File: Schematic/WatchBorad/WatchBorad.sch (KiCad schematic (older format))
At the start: 42 parts, among them IC1 TXS0108E, J1 Conn_01x06_Male, J2 Conn_01x09_Female, J3 USB_B_Mini, J4 Conn_01x10_Female, J5 Conn_01x06_Female, J6 Conn_01x04_Male, SW1 SW_Push, SW2 SW_Push, U1 E73-2G4M04S-52832, U2 FH26-13S-0.3SHW(05), U3 W25Q16BVSSIG, U5 MCP1700-3302E_SOT23, U6 MCP1700-1802E_SOT23, U7 LP2985-2.8, U8 MPU-9250

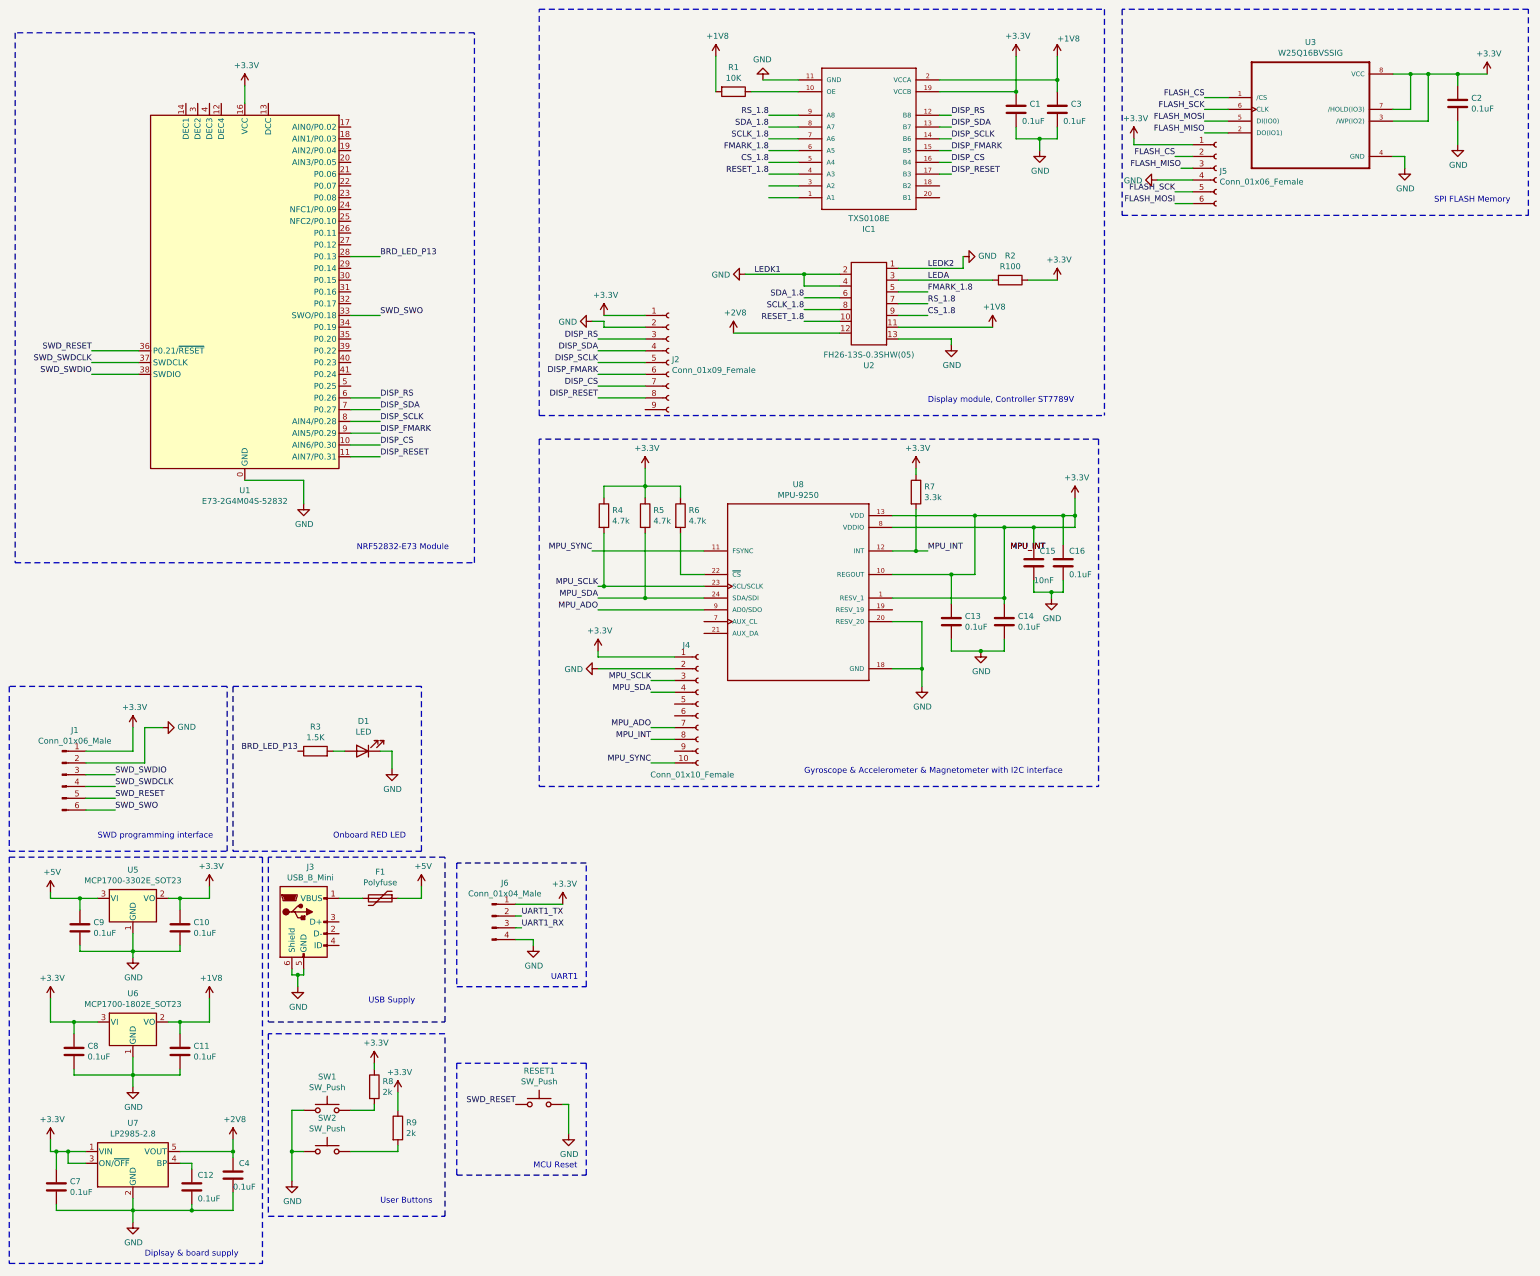
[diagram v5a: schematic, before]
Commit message: Added connectors for top-board
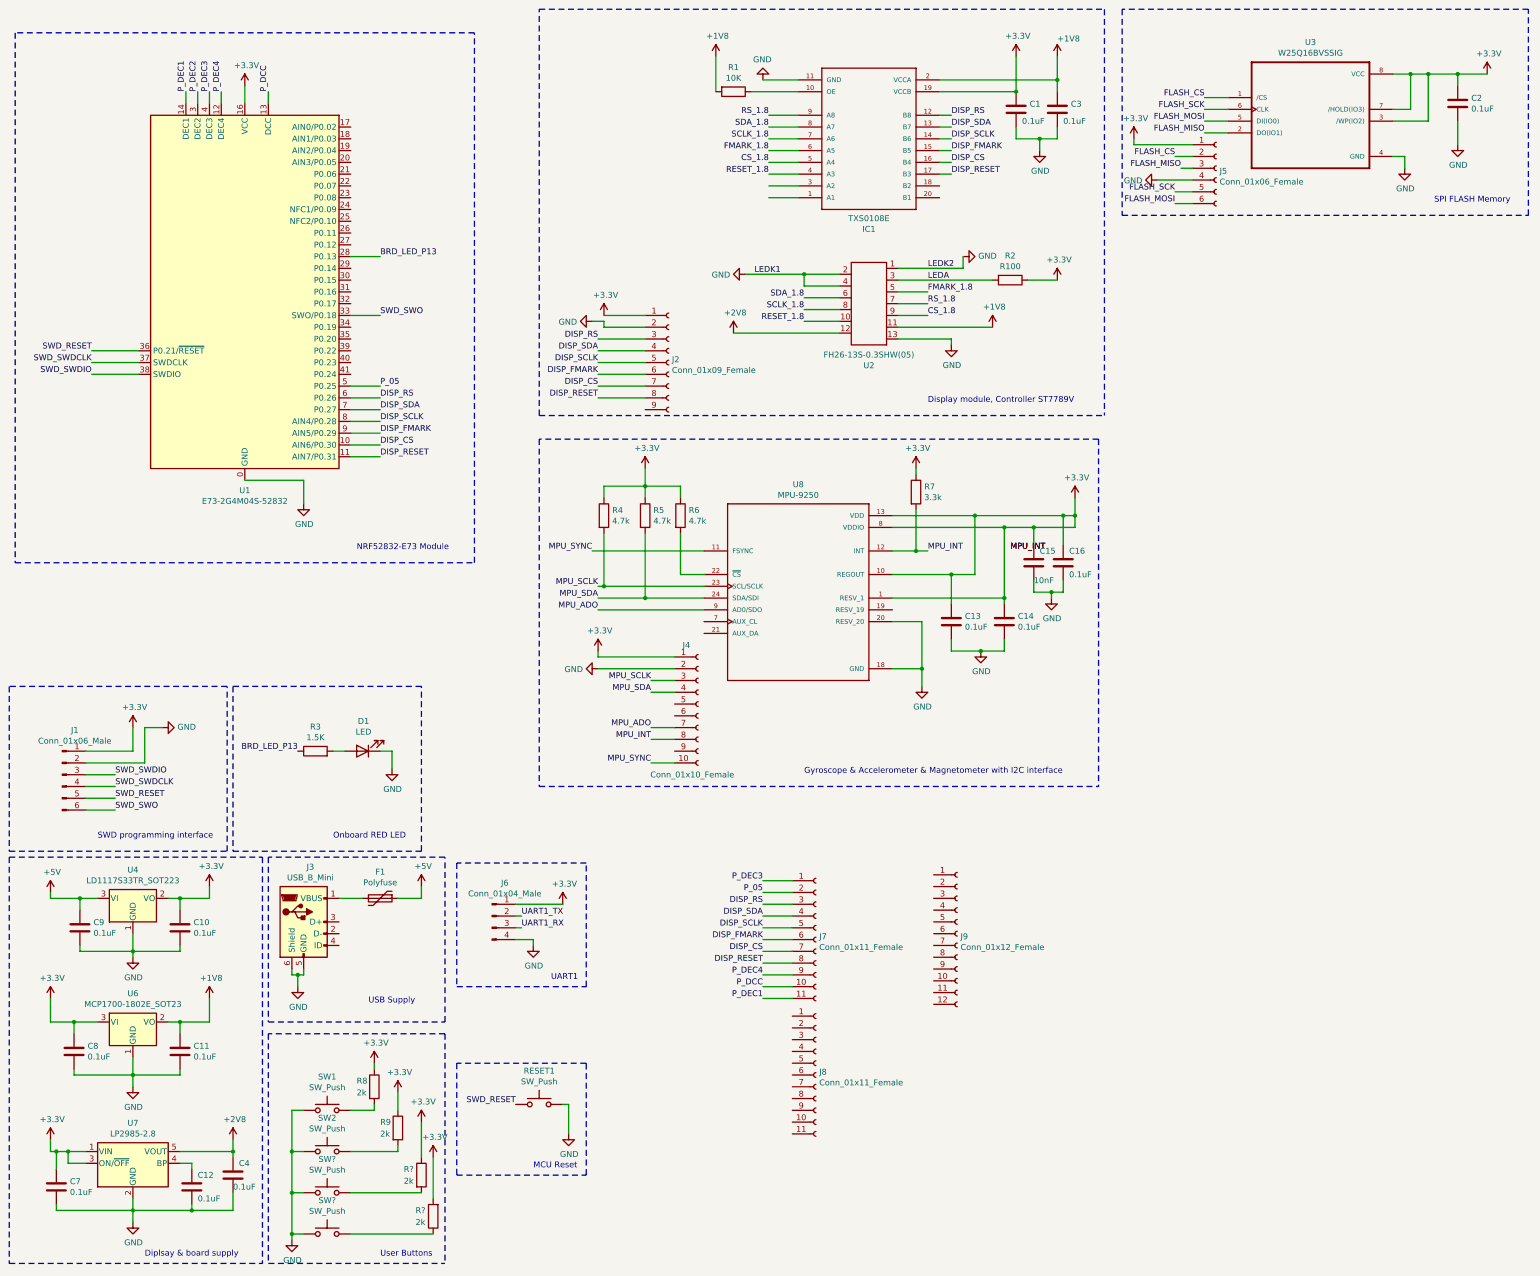
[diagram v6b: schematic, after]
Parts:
- removed U5: MCP1700-3302E_SOT23, Package_TO_SOT_SMD:SOT-23, symbol Regulator_Linear:MCP1700-3302E_SOT23
- added J7, J8: Conn_01x11_Female, Connector_PinSocket_2.54mm:PinSocket_1x11_P2.54mm_Vertical, symbol Connector:Conn_01x11_Female
- added J9: Conn_01x12_Female, Connector_PinSocket_2.54mm:PinSocket_1x12_P2.54mm_Vertical, symbol Connector:Conn_01x12_Female
- added R? (x2): 2k, Resistor_SMD:R_0805_2012Metric_Pad1.15x1.40mm_HandSolder, symbol Device:R
- added SW? (x2): SW_Push, Button_Switch_SMD:SW_SPST_SKQG_WithStem, symbol Switch:SW_Push
- added U4: LD1117S33TR_SOT223, Package_TO_SOT_SMD:SOT-223-3_TabPin2, symbol Regulator_Linear:LD1117S33TR_SOT223
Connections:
- net +3V3: now also R?.1, R?.2, U4.2 (VO)
- net +5V: now also U4.3 (VI)
- net DISP_CS: now also J7.7 (Pin_7)
- net DISP_FMARK: now also J7.6 (Pin_6)
- net DISP_RESET: now also J7.8 (Pin_8)
- net DISP_RS: now also J7.3 (Pin_3)
- net DISP_SCLK: now also J7.5 (Pin_5)
- net DISP_SDA: now also J7.4 (Pin_4)
- net GND: now also SW?.1, SW?.1, U4.1 (GND)
- net P_DEC4: now reaches U1.12 (DEC4)
- net P_DEC4: now also J7.9 (Pin_9)
- net P_DCC: now reaches U1.13 (DCC)
- net P_DCC: now also J7.10 (Pin_10)
- net P_DEC1: now reaches U1.14 (DEC1)
- net P_DEC1: now also J7.11 (Pin_11)
- net P_DEC2: now reaches U1.3 (DEC2)
- net P_DEC3: now reaches U1.4 (DEC3)
- net P_DEC3: now also J7.1 (Pin_1)
- net P_05: now reaches U1.5 (P0.25)
- net P_05: now also J7.2 (Pin_2)
- new net: R?.2, SW?.2
- new net: R?.1, SW?.2
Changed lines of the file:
@@
 EESchema Schematic File Version 4
+LIBS:WatchBorad-cache
 EELAYER 30 0
 EELAYER END
@@
 	1    0    0    -1
 $EndComp
-$Comp
-L Regulator_Linear:MCP1700-3302E_SOT23 U5
-U 1 1 5DBB69D4
-P 1650 8100
-F 0 "U5" H 1650 8342 50  0000 C CNN
-F 1 "MCP1700-3302E_SOT23" H 1650 8251 50  0000 C CNN
-F 2 "Package_TO_SOT_SMD:SOT-23" H 1650 8325 50  0001 C CNN
-F 3 "http://ww1.microchip.com/downloads/en/DeviceDoc/20001826C.pdf" H 1650 8100 50  0001 C CNN
-	1    1650 8100
-	1    0    0    -1
-$EndComp
 Wire Notes Line
 	4100 6300 2500 6300
@@
 U 1 1 5E659671
 P 3700 9700
-F 0 "R8" H 3770 9746 50  0000 L CNN
-F 1 "2k" H 3770 9655 50  0000 L CNN
+F 0 "R8" H 3550 9750 50  0000 L CNN
+F 1 "2k" H 3550 9650 50  0000 L CNN
 F 2 "Resistor_SMD:R_0805_2012Metric_Pad1.15x1.40mm_HandSolder" V 3630 9700 50  0001 C CNN
 F 3 "~" H 3700 9700 50  0001 C CNN
@@
 L power:GND #PWR0136
 U 1 1 5E67A207
-P 3000 10500
-F 0 "#PWR0136" H 3000 10250 50  0001 C CNN
-F 1 "GND" H 3005 10327 50  0000 C CNN
-F 2 "" H 3000 10500 50  0001 C CNN
-F 3 "" H 3000 10500 50  0001 C CNN
-	1    3000 10500
+P 3000 11000
+F 0 "#PWR0136" H 3000 10750 50  0001 C CNN
+F 1 "GND" H 3005 10827 50  0000 C CNN
+F 2 "" H 3000 11000 50  0001 C CNN
+F 3 "" H 3000 11000 50  0001 C CNN
+	1    3000 11000
 	1    0    0    -1
 $EndComp
@@
 U 1 1 5E6ACBD3
 P 3900 10050
-F 0 "R9" H 3970 10096 50  0000 L CNN
-F 1 "2k" H 3970 10005 50  0000 L CNN
+F 0 "R9" H 3750 10100 50  0000 L CNN
+F 1 "2k" H 3750 10000 50  0000 L CNN
 F 2 "Resistor_SMD:R_0805_2012Metric_Pad1.15x1.40mm_HandSolder" V 3830 10050 50  0001 C CNN
 F 3 "~" H 3900 10050 50  0001 C CNN
@@
 	3000 9900 3000 10250
 Connection ~ 3000 10250
-Wire Wire Line
-	3000 10250 3000 10500
 $Comp
 L power:GND #PWR0148
@@
 USB Supply
 Wire Notes Line
-	2800 9250 2800 10800
-Wire Notes Line
-	2800 10800 4300 10800
-Wire Notes Line
-	4300 10800 4300 9250
+	2800 11200 4300 11200
 Wire Notes Line
 	4300 9250 2800 9250
-Text Notes 3750 10700 0    50   ~ 0
+Text Notes 3750 11150 0    50   ~ 0
 User Buttons
 Wire Notes Line
@@
 Text Notes 3550 5150 0    50   ~ 0
 NRF52832-E73 Module
+$Comp
+L Regulator_Linear:LD1117S33TR_SOT223 U4
+U 1 1 5DB6B184
+P 1650 8100
+F 0 "U4" H 1650 8342 50  0000 C CNN
+F 1 "LD1117S33TR_SOT223" H 1650 8251 50  0000 C CNN
+F 2 "Package_TO_SOT_SMD:SOT-223-3_TabPin2" H 1650 8300 50  0001 C CNN
+F 3 "http://www.st.com/st-web-ui/static/active/en/resource/technical/document/datasheet/CD00000544.pdf" H 1750 7850 50  0001 C CNN
+	1    1650 8100
+	1    0    0    -1
+$EndComp
+$Comp
+L Connector:Conn_01x11_Female J7
+U 1 1 5DB988BA
+P 7450 8450
+F 0 "J7" H 7478 8476 50  0000 L CNN
+F 1 "Conn_01x11_Female" H 7478 8385 50  0000 L CNN
+F 2 "Connector_PinSocket_2.54mm:PinSocket_1x11_P2.54mm_Vertical" H 7450 8450 50  0001 C CNN
+F 3 "~" H 7450 8450 50  0001 C CNN
+	1    7450 8450
+	1    0    0    -1
+$EndComp
+$Comp
+L Connector:Conn_01x11_Female J8
+U 1 1 5DB9DBB8
+P 7450 9600
+F 0 "J8" H 7478 9626 50  0000 L CNN
+F 1 "Conn_01x11_Female" H 7478 9535 50  0000 L CNN
+F 2 "Connector_PinSocket_2.54mm:PinSocket_1x11_P2.54mm_Vertical" H 7450 9600 50  0001 C CNN
+F 3 "~" H 7450 9600 50  0001 C CNN
+	1    7450 9600
+	1    0    0    -1
+$EndComp
+$Comp
+L Connector:Conn_01x12_Female J9
+U 1 1 5DBA0F85
+P 8650 8400
+F 0 "J9" H 8678 8376 50  0000 L CNN
+F 1 "Conn_01x12_Female" H 8678 8285 50  0000 L CNN
+F 2 "Connector_PinSocket_2.54mm:PinSocket_1x12_P2.54mm_Vertical" H 8650 8400 50  0001 C CNN
+F 3 "~" H 8650 8400 50  0001 C CNN
+	1    8650 8400
+	1    0    0    -1
+$EndComp
+Text Label 2100 1250 1    50   ~ 0
+P_DEC1
+Wire Wire Line
+	2100 1250 2100 1350
+Text Label 2200 1250 1    50   ~ 0
+P_DEC2
+Text Label 2300 1250 1    50   ~ 0
+P_DEC3
+Text Label 2400 1250 1    50   ~ 0
+P_DEC4
+Wire Wire Line
+	2400 1250 2400 1350
+Wire Wire Line
+	2300 1250 2300 1350
+Wire Wire Line
+	2200 1350 2200 1250
+Text Label 7000 8950 2    50   ~ 0
+P_DEC1
+Wire Wire Line
+	7000 8950 7250 8950
+Text Label 2800 1250 1    50   ~ 0
+P_DCC
+Wire Wire Line
+	2800 1250 2800 1350
+Text Label 7000 8850 2    50   ~ 0
+P_DCC
+Wire Wire Line
+	7000 8850 7250 8850
+Text Label 7000 8750 2    50   ~ 0
+P_DEC4
+Wire Wire Line
+	7000 8750 7250 8750
+Text Label 7000 8650 2    50   ~ 0
+DISP_RESET
+Wire Wire Line
+	7000 8650 7250 8650
+Text Label 7000 8550 2    50   ~ 0
+DISP_CS
+Wire Wire Line
+	7000 8550 7250 8550
+Text Label 7000 8450 2    50   ~ 0
+DISP_FMARK
+Wire Wire Line
+	7000 8450 7250 8450
+Text Label 7000 8350 2    50   ~ 0
+DISP_SCLK
+Wire Wire Line
+	7000 8350 7250 8350
+Text Label 7000 8250 2    50   ~ 0
+DISP_SDA
+Wire Wire Line
+	7000 8250 7250 8250
+Text Label 7000 8150 2    50   ~ 0
+DISP_RS
+Wire Wire Line
+	7000 8150 7250 8150
+Text Label 3750 3750 0    50   ~ 0
+P_05
+Wire Wire Line
+	3500 3750 3750 3750
+Text Label 7000 8050 2    50   ~ 0
+P_05
+Wire Wire Line
+	7250 8050 7000 8050
+Text Label 7000 7950 2    50   ~ 0
+P_DEC3
+Wire Wire Line
+	7000 7950 7250 7950
+$Comp
+L Switch:SW_Push SW?
+U 1 1 5DD80B15
+P 3300 10600
+F 0 "SW?" H 3300 10885 50  0000 C CNN
+F 1 "SW_Push" H 3300 10794 50  0000 C CNN
+F 2 "Button_Switch_SMD:SW_SPST_SKQG_WithStem" H 3300 10800 50  0001 C CNN
+F 3 "~" H 3300 10800 50  0001 C CNN
+	1    3300 10600
+	1    0    0    -1
+$EndComp
+$Comp
+L Switch:SW_Push SW?
+U 1 1 5DD80B1B
+P 3300 10950
+F 0 "SW?" H 3300 11235 50  0000 C CNN
+F 1 "SW_Push" H 3300 11144 50  0000 C CNN
+F 2 "Button_Switch_SMD:SW_SPST_SKQG_WithStem" H 3300 11150 50  0001 C CNN
+F 3 "~" H 3300 11150 50  0001 C CNN
+	1    3300 10950
+	1    0    0    -1
+$EndComp
+Wire Wire Line
+	3000 10250 3000 10600
+Wire Notes Line
+	2800 9250 2800 11200
+Wire Notes Line
+	4300 9250 4300 11200
+$Comp
+L Device:R R?
+U 1 1 5DDFA376
+P 4100 10450
+F 0 "R?" H 3950 10500 50  0000 L CNN
+F 1 "2k" H 3950 10400 50  0000 L CNN
+F 2 "Resistor_SMD:R_0805_2012Metric_Pad1.15x1.40mm_HandSolder" V 4030 10450 50  0001 C CNN
+F 3 "~" H 4100 10450 50  0001 C CNN
+	1    4100 10450
+	1    0    0    -1
+$EndComp
+$Comp
+L Device:R R?
+U 1 1 5DDFB2BF
+P 4200 10800
+F 0 "R?" H 4350 10750 50  0000 R CNN
+F 1 "2k" H 4350 10850 50  0000 R CNN
+F 2 "Resistor_SMD:R_0805_2012Metric_Pad1.15x1.40mm_HandSolder" V 4130 10800 50  0001 C CNN
+F 3 "~" H 4200 10800 50  0001 C CNN
+	1    4200 10800
+	-1   0    0    1
+$EndComp
+Wire Wire Line
+	3500 10600 4100 10600
+Wire Wire Line
+	3500 10950 4200 10950
+Wire Wire Line
+	3100 10950 3000 10950
+Connection ~ 3000 10950
+Wire Wire Line
+	3000 10950 3000 11000
+Wire Wire Line
+	3100 10600 3000 10600
+Connection ~ 3000 10600
+Wire Wire Line
+	3000 10600 3000 10950
+$Comp
+L power:+3.3V #PWR?
+U 1 1 5DE52393
+P 4100 10000
+F 0 "#PWR?" H 4100 9850 50  0001 C CNN
+F 1 "+3.3V" H 4115 10173 50  0000 C CNN
+F 2 "" H 4100 10000 50  0001 C CNN
+F 3 "" H 4100 10000 50  0001 C CNN
+	1    4100 10000
+	1    0    0    -1
+$EndComp
+$Comp
+L power:+3.3V #PWR?
+U 1 1 5DE52E80
+P 4200 10300
+F 0 "#PWR?" H 4200 10150 50  0001 C CNN
+F 1 "+3.3V" H 4215 10473 50  0000 C CNN
+F 2 "" H 4200 10300 50  0001 C CNN
+F 3 "" H 4200 10300 50  0001 C CNN
+	1    4200 10300
+	1    0    0    -1
+$EndComp
+Wire Wire Line
+	4200 10300 4200 10650
+Wire Wire Line
+	4100 10300 4100 10000
 $EndSCHEMATC

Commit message: Added connectors for top-board-schematic
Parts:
- removed C1, C10, C11, C12, C13, C14, C16, C2, C3, C4, C7, C8, C9: 0.1uF, Capacitor_SMD:C_0805_2012Metric_Pad1.15x1.40mm_HandSolder, symbol Device:C
- removed C15: 10nF, Capacitor_SMD:C_0805_2012Metric_Pad1.15x1.40mm_HandSolder, symbol Device:C
- removed D1: LED, LED_SMD:LED_0805_2012Metric_Pad1.15x1.40mm_HandSolder, symbol Device:LED
- removed F1: Polyfuse, Fuse:Fuse_1206_3216Metric_Pad1.42x1.75mm_HandSolder, symbol Device:Polyfuse
- removed IC1: TXS0108E, TXS0108E:PW_R-PDSO-G20, symbol TXS0108E:TXS0108E
- removed J1: Conn_01x06_Male, Connector_PinHeader_2.54mm:PinHeader_1x06_P2.54mm_Vertical, symbol Connector:Conn_01x06_Male
- removed J2: Conn_01x09_Female, Connector_PinSocket_2.54mm:PinSocket_1x09_P2.54mm_Vertical, symbol Connector:Conn_01x09_Female
- removed J3: USB_B_Mini, Connector_USB:USB_Mini-B_Lumberg_2486_01_Horizontal, symbol Connector:USB_B_Mini
- removed J4: Conn_01x10_Female, Connector_PinSocket_2.54mm:PinSocket_1x10_P2.54mm_Vertical, symbol Connector:Conn_01x10_Female
- removed J5: Conn_01x06_Female, Connector_PinSocket_2.54mm:PinSocket_1x06_P2.54mm_Vertical, symbol Connector:Conn_01x06_Female
- removed J6: Conn_01x04_Male, Connector_PinHeader_2.54mm:PinHeader_1x04_P2.54mm_Vertical, symbol Connector:Conn_01x04_Male
- removed J7, J8: Conn_01x11_Female, Connector_PinSocket_2.54mm:PinSocket_1x11_P2.54mm_Vertical, symbol Connector:Conn_01x11_Female
- removed J9: Conn_01x12_Female, Connector_PinSocket_2.54mm:PinSocket_1x12_P2.54mm_Vertical, symbol Connector:Conn_01x12_Female
- removed R1: 10K, Resistor_SMD:R_0805_2012Metric_Pad1.15x1.40mm_HandSolder, symbol Device:R
- removed R2: R100, Resistor_SMD:R_0805_2012Metric_Pad1.15x1.40mm_HandSolder, symbol Device:R
- removed R3: 1.5K, Resistor_SMD:R_0805_2012Metric_Pad1.15x1.40mm_HandSolder, symbol Device:R
- removed R4, R5, R6: 4.7k, Resistor_SMD:R_0805_2012Metric_Pad1.15x1.40mm_HandSolder, symbol Device:R
- removed R7: 3.3k, Resistor_SMD:R_0805_2012Metric_Pad1.15x1.40mm_HandSolder, symbol Device:R
- removed R8, R9, R? (x2): 2k, Resistor_SMD:R_0805_2012Metric_Pad1.15x1.40mm_HandSolder, symbol Device:R
- removed RESET1, SW1, SW2, SW? (x2): SW_Push, Button_Switch_SMD:SW_SPST_SKQG_WithStem, symbol Switch:SW_Push
- removed U1: E73-2G4M04S-52832, RF_Module:E73-2G4M04S, symbol RF_Module:E73-2G4M04S-52832
- removed U2: FH26-13S-0.3SHW(05), FH26W-13S-0:FH26-13S-0.3SHW(05), symbol Hirose_connectors:FH26-13S-0.3SHW(05)
- removed U3: W25Q16BVSSIG, W25Q16BVSSIG:SOIC127P790X216-8N, symbol W25Q16BVSSIG:W25Q16BVSSIG
- removed U4: LD1117S33TR_SOT223, Package_TO_SOT_SMD:SOT-223-3_TabPin2, symbol Regulator_Linear:LD1117S33TR_SOT223
- removed U6: MCP1700-1802E_SOT23, Package_TO_SOT_SMD:SOT-23, symbol Regulator_Linear:MCP1700-1802E_SOT23
- removed U7: LP2985-2.8, Package_TO_SOT_SMD:SOT-23-5, symbol Regulator_Linear:LP2985-2.8
- removed U8: MPU-9250, QFN40P300X300X105-24N, symbol MPU-9250:MPU-9250
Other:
- note removed: "Diplsay & board supply"
- note removed: "Display module, Controller ST7789V"
- note removed: "Gyroscope & Accelerometer & Magnetometer with I2C interface"
- note removed: "MCU Reset"
- note removed: "NRF52832-E73 Module"
- note removed: "Onboard RED LED"
- note removed: "SPI FLASH Memory\n"
- note removed: "SWD programming interface"
- note removed: "UART1"
- note removed: "USB Supply"
- note removed: "User Buttons"
